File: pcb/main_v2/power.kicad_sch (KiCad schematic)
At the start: 33 parts, among them IC201 AP22811AW5-7, J201 USB_A, SW201 SW_DIP_x01, U201 LT3042xMSE

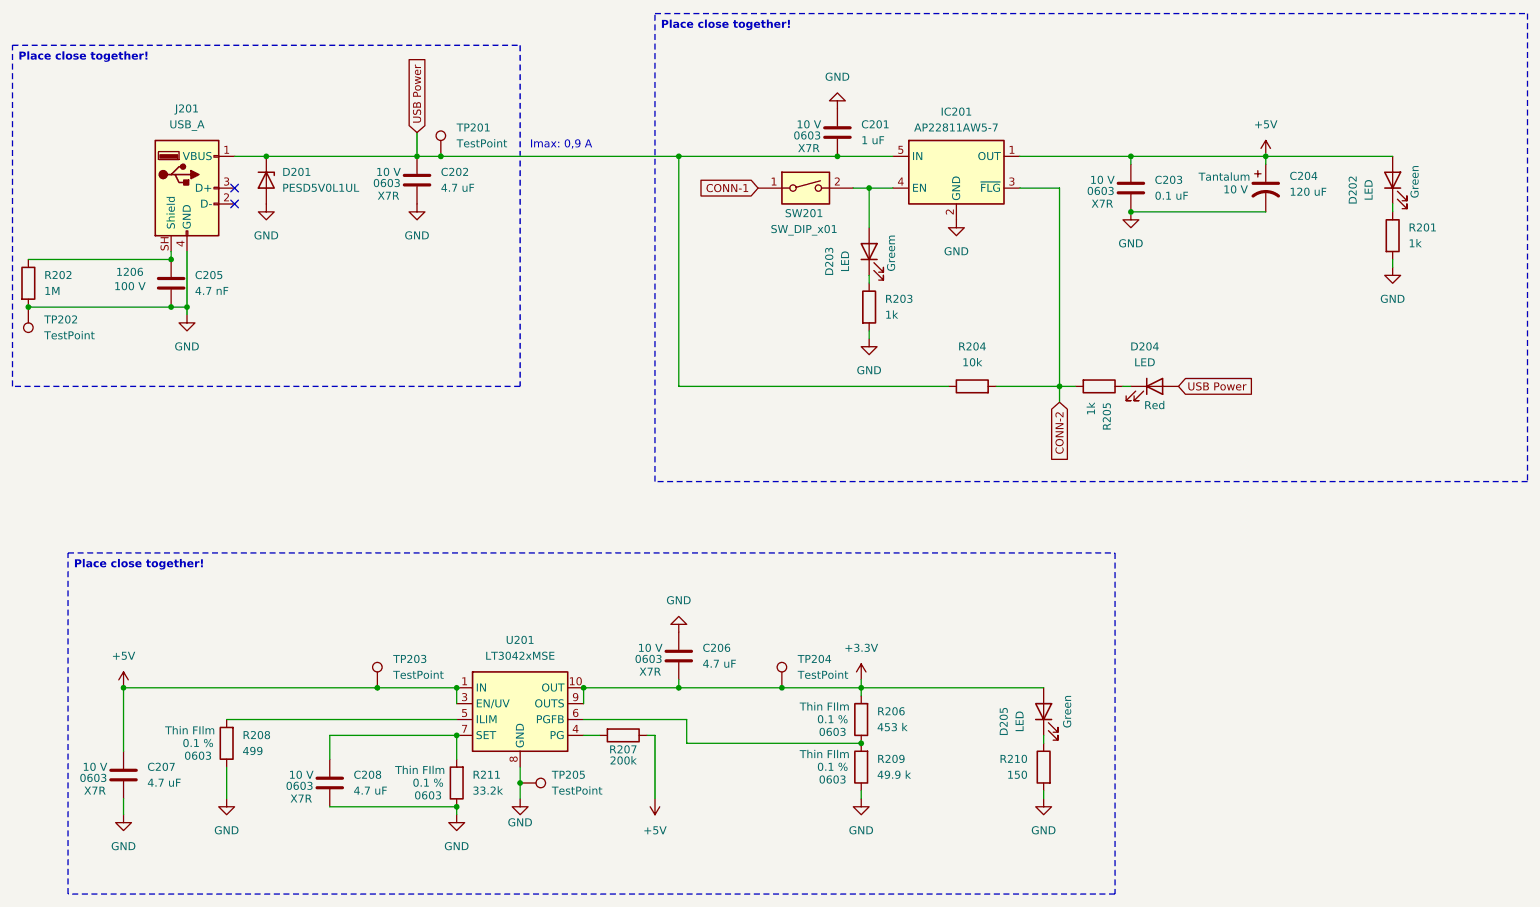
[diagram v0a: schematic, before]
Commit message: updated layout
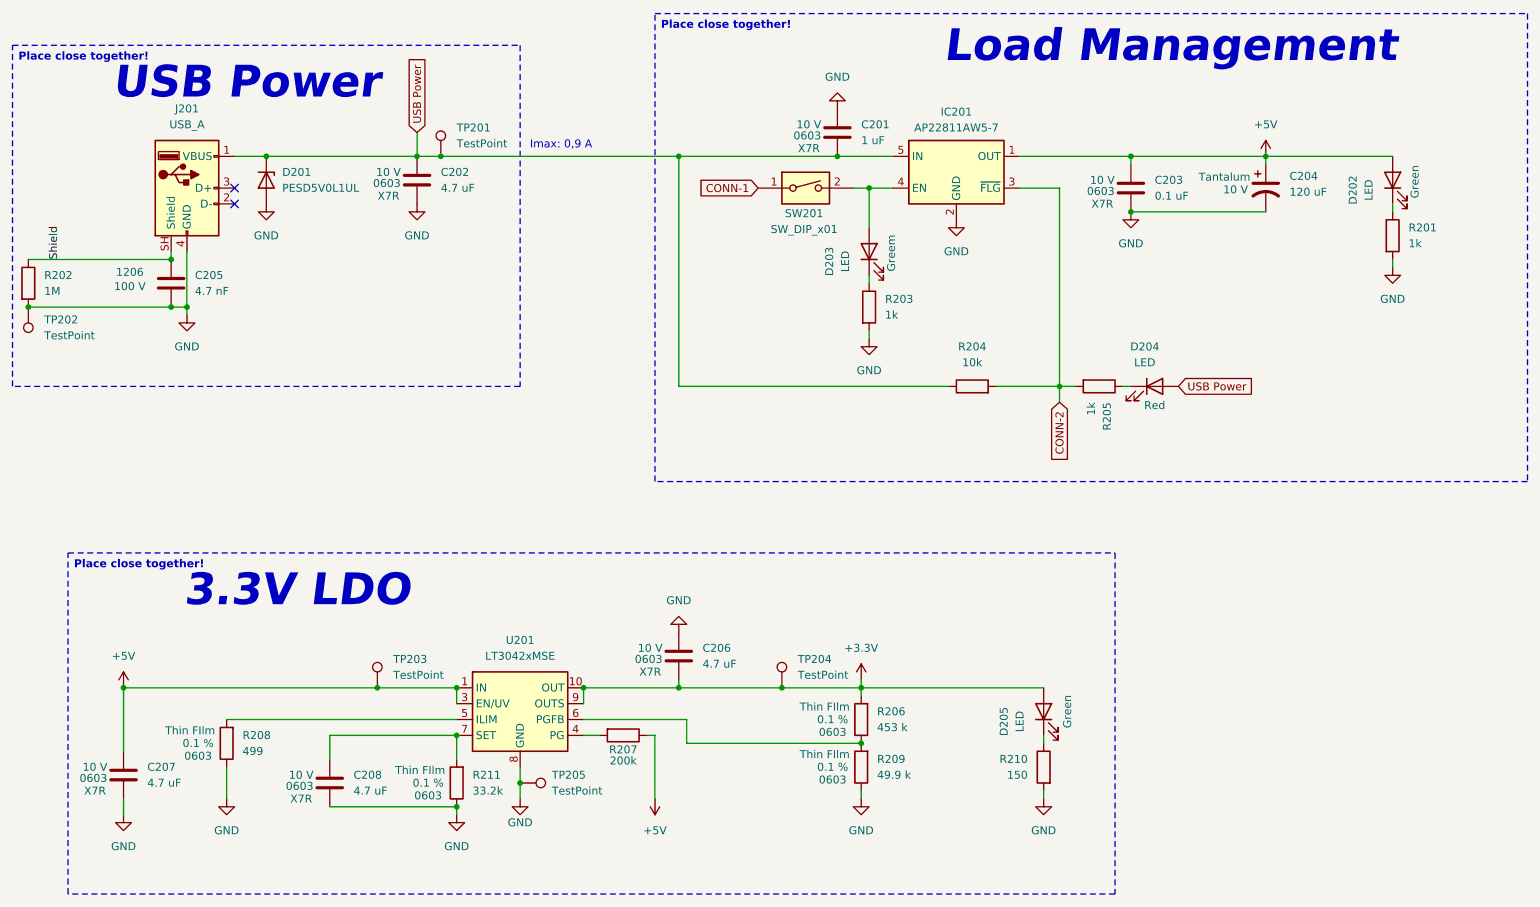
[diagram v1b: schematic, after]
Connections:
- net Shield: now reaches C205.1, J201.SH (Shield), R202.1
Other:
- note added: "3.3V LDO"
- note added: "Load Management"
- note added: "USB Power"
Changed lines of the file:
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@@
 	(generator_version "10.0")
 	(paper "A4")
+	(text "USB Power"
+		(exclude_from_sim no)
+		(at 41.402 31.496 0)
+		(effects
+			(font
+				(size 5.08 5.08)
+				(thickness 0.254)
+				(bold yes)
+				(italic yes)
+				(color 62 180 4 1)
+			)
+			(justify left)
+		)
+	)
+	(text "Load Management"
+		(exclude_from_sim no)
+		(at 174.498 25.654 0)
+		(effects
+			(font
+				(size 5.08 5.08)
+				(thickness 0.254)
+				(bold yes)
+				(italic yes)
+				(color 62 180 4 1)
+			)
+			(justify left)
+		)
+	)
+	(text "3.3V LDO"
+		(exclude_from_sim no)
+		(at 52.832 112.776 0)
+		(effects
+			(font
+				(size 5.08 5.08)
+				(thickness 0.254)
+				(bold yes)
+				(italic yes)
+				(color 62 180 4 1)
+			)
+			(justify left)
+		)
+	)
 	(text "Imax: 0,9 A"
 		(exclude_from_sim no)
@@
 		)
 	)
+	(label "Shield"
+		(at 33.02 59.69 90)
+		(fields_autoplaced yes)
+		(effects
+			(font
+				(size 1.27 1.27)
+			)
+			(justify left bottom)
+		)
+		(property "Net Class" "GND"
+			(at 34.29 59.69 90)
+			(show_name no)
+			(do_not_autoplace no)
+			(effects
+				(font
+					(size 1.27 1.27)
+					(italic yes)
+				)
+				(justify left)
+			)
+		)
+	)
